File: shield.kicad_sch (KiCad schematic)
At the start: 0 parts

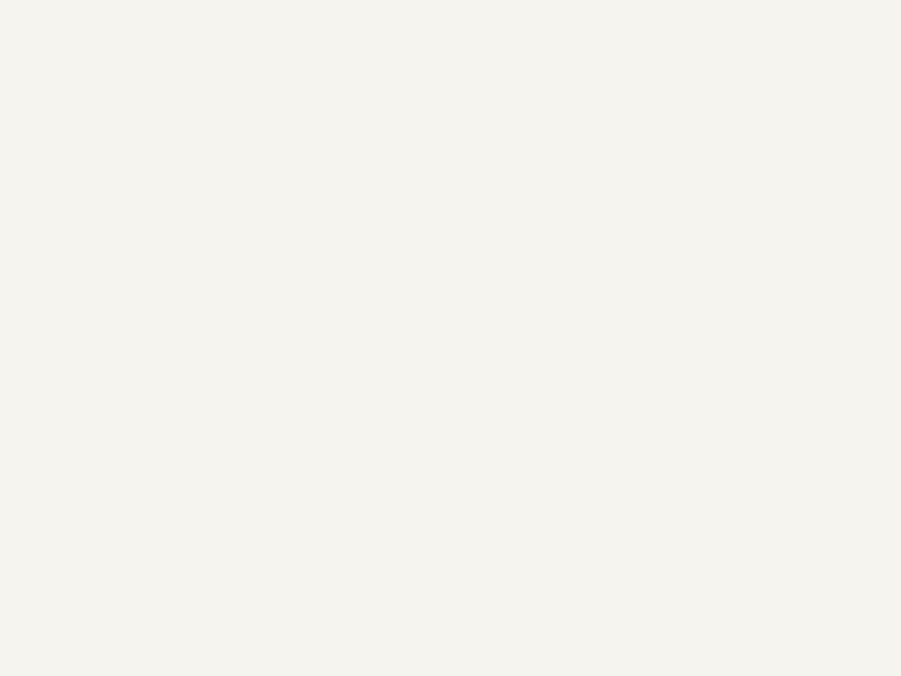
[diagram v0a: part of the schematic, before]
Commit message: Ajoute l'alimentation USB-C Power Delivery des cartes filles (STUSB4531QTR)
Nouvelle feuille usb_pd.kicad_sch : recepteur USB-C Wurth 632722100213,
STUSB4531QTR (negociation PD autonome, 100W/20V/5A), MOSFET P
SQJ459EP-T2_GE3 comme unique interrupteur de puissance (pas d'eFuse),
protections TVS, 2 LED de statut, sortie vers les cartes filles en
daisy chain. Supervision I2C par l'ESP32 (GPIO21/22/23), distincte du
bus I2C des nappes qui reste au C2000.

Deuxieme entree d'alimentation, separee du 11-25V existant. HV_EN et
Discharge (nappe GPIO-1) ne sont pas reutilises : le STUSB4531QTR gere
sa propre coupure/decharge en autonome. Decision #23 pour le detail
complet (composants, justifications, bugs trouves et corriges pendant
la verification ERC).

Co-Authored-By: Claude Sonnet 5 <noreply@anthropic.com>
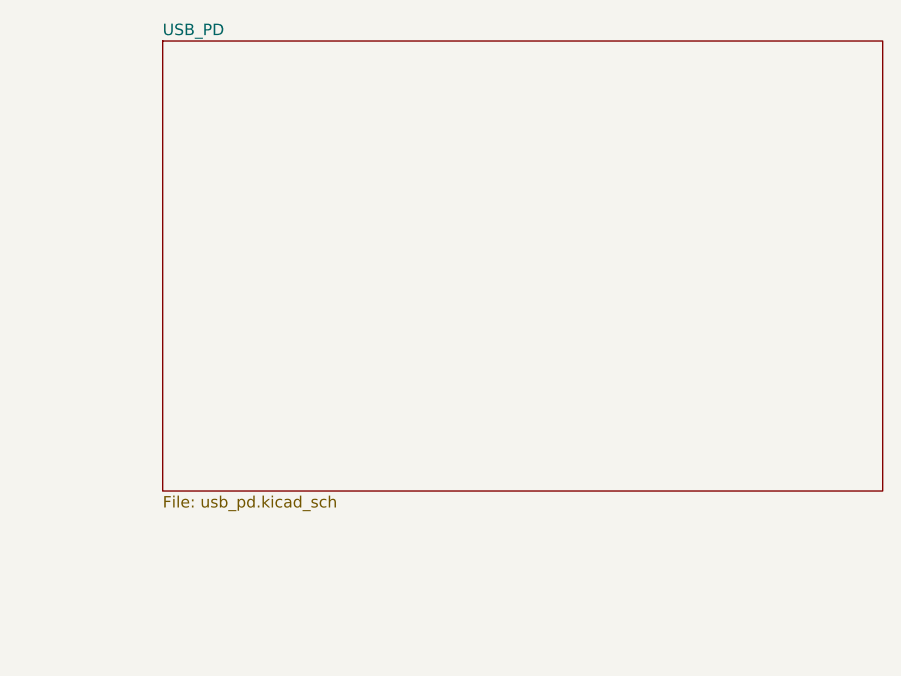
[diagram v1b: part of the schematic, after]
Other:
- added sheet USB_PD (usb_pd.kicad_sch)
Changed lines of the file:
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@@
+		)
+	)
+	(sheet
+		(at 320 20)
+		(size 80 50)
+		(exclude_from_sim no)
+		(in_bom yes)
+		(on_board yes)
+		(dnp no)
+		(fields_autoplaced yes)
+		(stroke
+			(width 0.1524)
+			(type solid)
+		)
+		(fill
+			(color 0 0 0 0)
+		)
+		(property "Sheetname" "USB_PD"
+			(at 320 19.5 0)
+			(show_name no)
+			(do_not_autoplace no)
+			(effects
+				(font
+					(size 1.27 1.27)
+				)
+				(justify left bottom)
+			)
+		)
+		(property "Sheetfile" "usb_pd.kicad_sch"
+			(at 320 70.5 0)
+			(show_name no)
+			(do_not_autoplace no)
+			(effects
+				(font
+					(size 1.27 1.27)
+				)
+				(justify left top)
+			)
+		)
+		(instances
+			(project "shield"
+				(path "/3e79b37e-13ed-4a43-b954-3b2f3b716c2c"
+					(page "9")
+				)
+			)
 		)
 	)
